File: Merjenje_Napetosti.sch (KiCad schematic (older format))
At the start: 6 parts

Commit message: Dodano vezje za OC_trip pri merjenju toka
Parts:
- removed U?: MCP6001R, Package_TO_SOT_SMD:SOT-23-5, symbol Amplifier_Operational:MCP6001R
- added U?: MCP601R, Package_TO_SOT_SMD:SOT-23-5, symbol Amplifier_Operational:MCP601R
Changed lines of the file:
@@
 $Descr A4 11693 8268
 encoding utf-8
-Sheet 4 4
+Sheet 4 5
 Title ""
 Date ""
@@
 	3500 2800 4250 2800
 $Comp
-L Amplifier_Operational:MCP6001R U?
-U 1 1 5BCCC475
-P 5050 2450
-F 0 "U?" H 5391 2496 50  0000 L CNN
-F 1 "MCP6001R" H 5391 2405 50  0000 L CNN
-F 2 "Package_TO_SOT_SMD:SOT-23-5" H 5050 2450 50  0001 C CNN
-F 3 "http://ww1.microchip.com/downloads/en/DeviceDoc/21733j.pdf" H 5050 2650 50  0001 C CNN
-	1    5050 2450
-	1    0    0    -1
-$EndComp
-$Comp
 L Passives:GND #PWR?
 U 1 1 5BCCC5E3
@@
 Wire Wire Line
 	5450 2450 5800 2450
+$Comp
+L Amplifier_Operational:MCP601R U?
+U 1 1 5BCDCCEB
+P 5050 2450
+F 0 "U?" H 5391 2496 50  0000 L CNN
+F 1 "MCP601R" H 5391 2405 50  0000 L CNN
+F 2 "Package_TO_SOT_SMD:SOT-23-5" H 5050 2450 50  0001 C CNN
+F 3 "http://ww1.microchip.com/downloads/en/DeviceDoc/21314g.pdf" H 5050 2650 50  0001 C CNN
+	1    5050 2450
+	1    0    0    -1
+$EndComp
 $EndSCHEMATC

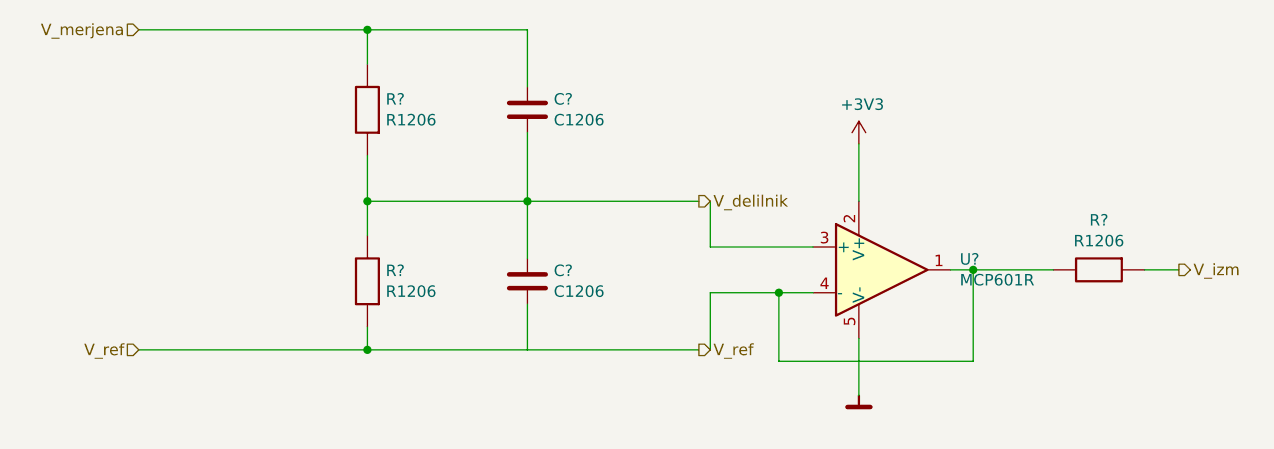
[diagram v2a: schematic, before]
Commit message: Naredil še sheet napajanje in popravil merilnik napetosti pri merjenju fazne napetosti
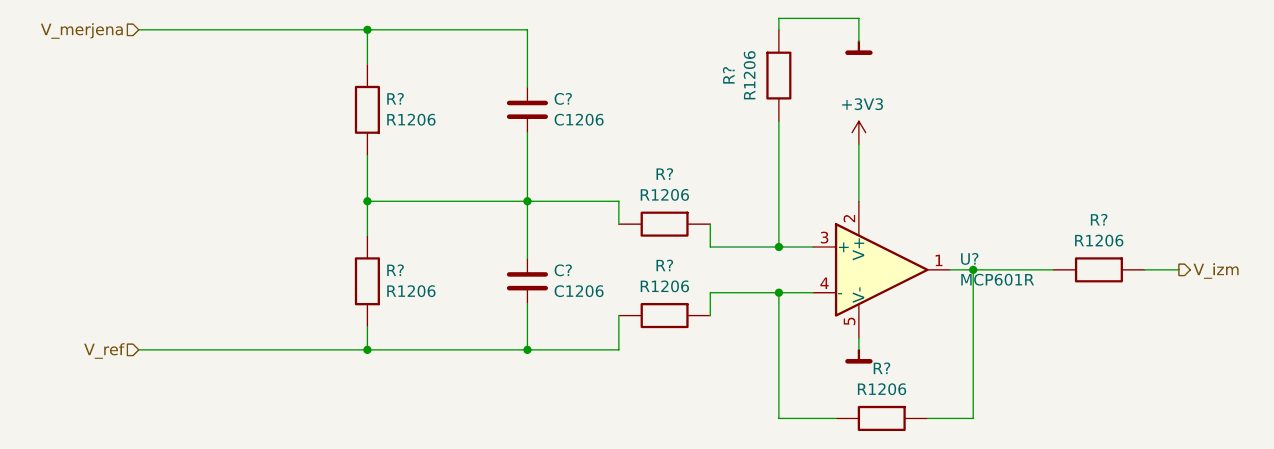
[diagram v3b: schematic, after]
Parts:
- removed U?: MCP601R, Package_TO_SOT_SMD:SOT-23-5, symbol Amplifier_Operational:MCP601R
- added R? (x4): R1206, Passives:R1206M, symbol Passives:R1206
- added U?: MCP601R, Package_TO_SOT_SMD:SOT-23-5, symbol Amplifier_Operational:MCP601R
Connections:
- net labels removed: V_delilnik
- wire segments 28 -> 36
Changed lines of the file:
@@
 $Descr A4 11693 8268
 encoding utf-8
-Sheet 4 7
+Sheet 4 9
 Title ""
 Date ""
@@
 U 1 1 5BCCBE50
 P 2800 1750
+AR Path="/5BC702AD/5BCCBCD0/5BCCBE50" Ref="R?"  Part="1"
+AR Path="/5BD3A78C/5BCCBE50" Ref="R?"  Part="1"
 F 0 "R?" V 2754 1830 50  0000 L CNN
 F 1 "R1206" V 2845 1830 50  0000 L CNN
@@
 U 1 1 5BCCBFA4
 P 2800 2500
+AR Path="/5BC702AD/5BCCBCD0/5BCCBFA4" Ref="R?"  Part="1"
+AR Path="/5BD3A78C/5BCCBFA4" Ref="R?"  Part="1"
 F 0 "R?" V 2754 2580 50  0000 L CNN
 F 1 "R1206" V 2845 2580 50  0000 L CNN
@@
 U 1 1 5BCCBFDD
 P 3500 1750
+AR Path="/5BC702AD/5BCCBCD0/5BCCBFDD" Ref="C?"  Part="1"
+AR Path="/5BD3A78C/5BCCBFDD" Ref="C?"  Part="1"
 F 0 "C?" H 3615 1796 50  0000 L CNN
 F 1 "C1206" H 3615 1705 50  0000 L CNN
@@
 U 1 1 5BCCC057
 P 3500 2500
+AR Path="/5BC702AD/5BCCBCD0/5BCCC057" Ref="C?"  Part="1"
+AR Path="/5BD3A78C/5BCCC057" Ref="C?"  Part="1"
 F 0 "C?" H 3615 2546 50  0000 L CNN
 F 1 "C1206" H 3615 2455 50  0000 L CNN
@@
 Wire Wire Line
 	3500 2800 3500 2600
-Text HLabel 1800 1400 0    50   Input ~ 0
-V_merjena
 Wire Wire Line
 	1800 1400 2800 1400
 Connection ~ 2800 1400
-Text HLabel 1800 2800 0    50   Input ~ 0
-V_ref
 Wire Wire Line
 	2800 2800 1800 2800
@@
 Wire Wire Line
 	3500 2150 3500 2400
-Text HLabel 4250 2150 2    50   Output ~ 0
-V_delilnik
-Wire Wire Line
-	3500 2150 4250 2150
-Text HLabel 4250 2800 2    50   Output ~ 0
-V_ref
-Wire Wire Line
-	3500 2800 4250 2800
-$Comp
-L Passives:GND #PWR?
-U 1 1 5BCCC5E3
-P 4950 3000
-F 0 "#PWR?" H 4950 2850 50  0001 C CNN
-F 1 "GND" H 5100 2950 50  0001 C CNN
-F 2 "" H 4950 3000 50  0001 C CNN
-F 3 "" H 4950 3000 50  0001 C CNN
-	1    4950 3000
-	1    0    0    -1
-$EndComp
-Wire Wire Line
-	4950 2750 4950 3000
-Wire Wire Line
-	4300 2800 4300 2550
-Wire Wire Line
-	4300 2550 4600 2550
-Wire Wire Line
-	4300 2150 4300 2350
-Wire Wire Line
-	4300 2350 4750 2350
 $Comp
 L Passives:R1206 R?
 U 1 1 5BCCC942
 P 6000 2450
+AR Path="/5BC702AD/5BCCBCD0/5BCCC942" Ref="R?"  Part="1"
+AR Path="/5BD3A78C/5BCCC942" Ref="R?"  Part="1"
 F 0 "R?" H 6000 2667 50  0000 C CNN
 F 1 "R1206" H 6000 2576 50  0000 C CNN
@@
 	1    0    0    -1
 $EndComp
-Wire Wire Line
-	5350 2450 5450 2450
 Text HLabel 6350 2450 2    50   Output ~ 0
 V_izm
 Wire Wire Line
 	6200 2450 6350 2450
+Text HLabel 1800 2800 0    50   Input ~ 0
+V_ref
+Text HLabel 1800 1400 0    50   Input ~ 0
+V_merjena
+$Comp
+L Passives:GND #PWR?
+U 1 1 5BD45445
+P 4950 2800
+AR Path="/5BC702AD/5BCCBCD0/5BD45445" Ref="#PWR?"  Part="1"
+AR Path="/5BD3A78C/5BD45445" Ref="#PWR?"  Part="1"
+F 0 "#PWR?" H 4950 2650 50  0001 C CNN
+F 1 "GND" H 5100 2750 50  0001 C CNN
+F 2 "" H 4950 2800 50  0001 C CNN
+F 3 "" H 4950 2800 50  0001 C CNN
+	1    4950 2800
+	1    0    0    -1
+$EndComp
+Wire Wire Line
+	4300 2550 4600 2550
+Wire Wire Line
+	4300 2350 4600 2350
+Wire Wire Line
+	5350 2450 5450 2450
 $Comp
 L power:+3V3 #PWR?
-U 1 1 5BCCD420
+U 1 1 5BD4544E
 P 4950 1900
+AR Path="/5BC702AD/5BCCBCD0/5BD4544E" Ref="#PWR?"  Part="1"
+AR Path="/5BD3A78C/5BD4544E" Ref="#PWR?"  Part="1"
 F 0 "#PWR?" H 4950 1750 50  0001 C CNN
 F 1 "+3V3" H 4965 2073 50  0000 C CNN
@@
 Wire Wire Line
 	4950 1900 4950 2150
-Wire Wire Line
-	4600 2550 4600 2850
-Wire Wire Line
-	4600 2850 5450 2850
-Wire Wire Line
-	5450 2850 5450 2450
 Connection ~ 4600 2550
 Wire Wire Line
@@
 $Comp
 L Amplifier_Operational:MCP601R U?
-U 1 1 5BCDCCEB
+U 1 1 5BD45459
 P 5050 2450
+AR Path="/5BC702AD/5BCCBCD0/5BD45459" Ref="U?"  Part="1"
+AR Path="/5BD3A78C/5BD45459" Ref="U?"  Part="1"
 F 0 "U?" H 5391 2496 50  0000 L CNN
 F 1 "MCP601R" H 5391 2405 50  0000 L CNN
@@
 	1    0    0    -1
 $EndComp
+$Comp
+L Passives:R1206 R?
+U 1 1 5BD45460
+P 4100 2250
+AR Path="/5BC702AD/5BCCBCD0/5BD45460" Ref="R?"  Part="1"
+AR Path="/5BD3A78C/5BD45460" Ref="R?"  Part="1"
+F 0 "R?" H 4100 2467 50  0000 C CNN
+F 1 "R1206" H 4100 2376 50  0000 C CNN
+F 2 "Passives:R1206M" H 4000 2150 50  0001 L CNN
+F 3 "" H 4100 2250 50  0001 C CNN
+	1    4100 2250
+	1    0    0    -1
+$EndComp
+$Comp
+L Passives:R1206 R?
+U 1 1 5BD45468
+P 4600 1600
+AR Path="/5BC702AD/5BCCBCD0/5BD45468" Ref="R?"  Part="1"
+AR Path="/5BD3A78C/5BD45468" Ref="R?"  Part="1"
+F 0 "R?" H 4600 1817 50  0000 C CNN
+F 1 "R1206" H 4600 1726 50  0000 C CNN
+F 2 "Passives:R1206M" H 4500 1500 50  0001 L CNN
+F 3 "" H 4600 1600 50  0001 C CNN
+	1    4600 1600
+	0    -1   -1   0
+$EndComp
+Wire Wire Line
+	4600 2350 4600 1800
+Connection ~ 4600 2350
+Wire Wire Line
+	4600 2350 4750 2350
+$Comp
+L Passives:GND #PWR?
+U 1 1 5BD45472
+P 4950 1450
+F 0 "#PWR?" H 4950 1300 50  0001 C CNN
+F 1 "GND" H 5100 1400 50  0001 C CNN
+F 2 "" H 4950 1450 50  0001 C CNN
+F 3 "" H 4950 1450 50  0001 C CNN
+	1    4950 1450
+	1    0    0    -1
+$EndComp
+Wire Wire Line
+	4950 1450 4950 1350
+Wire Wire Line
+	4950 1350 4600 1350
+Wire Wire Line
+	4600 1350 4600 1400
+$Comp
+L Passives:R1206 R?
+U 1 1 5BD4547B
+P 5050 3100
+AR Path="/5BC702AD/5BCCBCD0/5BD4547B" Ref="R?"  Part="1"
+AR Path="/5BD3A78C/5BD4547B" Ref="R?"  Part="1"
+F 0 "R?" H 5050 3317 50  0000 C CNN
+F 1 "R1206" H 5050 3226 50  0000 C CNN
+F 2 "Passives:R1206M" H 4950 3000 50  0001 L CNN
+F 3 "" H 5050 3100 50  0001 C CNN
+	1    5050 3100
+	1    0    0    -1
+$EndComp
+Wire Wire Line
+	4850 3100 4600 3100
+Wire Wire Line
+	5450 3100 5250 3100
+Wire Wire Line
+	4950 2800 4950 2750
+Wire Wire Line
+	4600 2550 4600 3100
+Wire Wire Line
+	5450 2450 5450 3100
+$Comp
+L Passives:R1206 R?
+U 1 1 5BD45487
+P 4100 2650
+AR Path="/5BC702AD/5BCCBCD0/5BD45487" Ref="R?"  Part="1"
+AR Path="/5BD3A78C/5BD45487" Ref="R?"  Part="1"
+F 0 "R?" H 4100 2867 50  0000 C CNN
+F 1 "R1206" H 4100 2776 50  0000 C CNN
+F 2 "Passives:R1206M" H 4000 2550 50  0001 L CNN
+F 3 "" H 4100 2650 50  0001 C CNN
+	1    4100 2650
+	1    0    0    -1
+$EndComp
+Wire Wire Line
+	4300 2350 4300 2250
+Wire Wire Line
+	4300 2650 4300 2550
+Wire Wire Line
+	3500 2150 3900 2150
+Wire Wire Line
+	3900 2150 3900 2250
+Wire Wire Line
+	3500 2800 3900 2800
+Wire Wire Line
+	3900 2800 3900 2650
+Connection ~ 3500 2800
 $EndSCHEMATC

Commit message: Dodal nekaj blikornih kondenzatorjev
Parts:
- removed R? (x4): R1206, Passives:R1206M, symbol Passives:R1206
- added C?: C1206, Passives:C1206M, symbol Passives:C1206
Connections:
- net V_ref is gone; now on net GND: C?.2, R?.2
- net +3V3: now also C?.1
- net GND: now also C?.2
- net at C?.1, C?.2, R?.1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: now also U?.3 (+)
- net at R?.1, U?.1: now also U?.4 (-)
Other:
- moved on the sheet: R?, U?
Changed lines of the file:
@@
 L Passives:R1206 R?
 U 1 1 5BCCC942
-P 6000 2450
+P 6000 2250
 AR Path="/5BC702AD/5BCCBCD0/5BCCC942" Ref="R?"  Part="1"
 AR Path="/5BD3A78C/5BCCC942" Ref="R?"  Part="1"
-F 0 "R?" H 6000 2667 50  0000 C CNN
-F 1 "R1206" H 6000 2576 50  0000 C CNN
-F 2 "Passives:R1206M" H 5900 2350 50  0001 L CNN
-F 3 "" H 6000 2450 50  0001 C CNN
-	1    6000 2450
+F 0 "R?" H 6000 2467 50  0000 C CNN
+F 1 "R1206" H 6000 2376 50  0000 C CNN
+F 2 "Passives:R1206M" H 5900 2150 50  0001 L CNN
+F 3 "" H 6000 2250 50  0001 C CNN
+	1    6000 2250
 	1    0    0    -1
 $EndComp
-Text HLabel 6350 2450 2    50   Output ~ 0
+Text HLabel 6350 2250 2    50   Output ~ 0
 V_izm
 Wire Wire Line
-	6200 2450 6350 2450
-Text HLabel 1800 2800 0    50   Input ~ 0
-V_ref
+	6200 2250 6350 2250
 Text HLabel 1800 1400 0    50   Input ~ 0
 V_merjena
@@
 $EndComp
 Wire Wire Line
-	4300 2550 4600 2550
-Wire Wire Line
-	4300 2350 4600 2350
-Wire Wire Line
-	5350 2450 5450 2450
+	5350 2250 5450 2250
 $Comp
 L power:+3V3 #PWR?
 U 1 1 5BD4544E
-P 4950 1900
+P 4950 1700
 AR Path="/5BC702AD/5BCCBCD0/5BD4544E" Ref="#PWR?"  Part="1"
 AR Path="/5BD3A78C/5BD4544E" Ref="#PWR?"  Part="1"
-F 0 "#PWR?" H 4950 1750 50  0001 C CNN
-F 1 "+3V3" H 4965 2073 50  0000 C CNN
-F 2 "" H 4950 1900 50  0001 C CNN
-F 3 "" H 4950 1900 50  0001 C CNN
-	1    4950 1900
+F 0 "#PWR?" H 4950 1550 50  0001 C CNN
+F 1 "+3V3" H 4965 1873 50  0000 C CNN
+F 2 "" H 4950 1700 50  0001 C CNN
+F 3 "" H 4950 1700 50  0001 C CNN
+	1    4950 1700
 	1    0    0    -1
 $EndComp
 Wire Wire Line
-	4950 1900 4950 2150
-Connection ~ 4600 2550
+	4950 1700 4950 1850
 Wire Wire Line
-	4600 2550 4750 2550
-Connection ~ 5450 2450
+	4600 2350 4750 2350
+Connection ~ 5450 2250
 Wire Wire Line
-	5450 2450 5800 2450
+	5450 2250 5800 2250
 $Comp
 L Amplifier_Operational:MCP601R U?
 U 1 1 5BD45459
-P 5050 2450
+P 5050 2250
 AR Path="/5BC702AD/5BCCBCD0/5BD45459" Ref="U?"  Part="1"
 AR Path="/5BD3A78C/5BD45459" Ref="U?"  Part="1"
-F 0 "U?" H 5391 2496 50  0000 L CNN
-F 1 "MCP601R" H 5391 2405 50  0000 L CNN
-F 2 "Package_TO_SOT_SMD:SOT-23-5" H 5050 2450 50  0001 C CNN
-F 3 "http://ww1.microchip.com/downloads/en/DeviceDoc/21314g.pdf" H 5050 2650 50  0001 C CNN
-	1    5050 2450
-	1    0    0    -1
-$EndComp
-$Comp
-L Passives:R1206 R?
-U 1 1 5BD45460
-P 4100 2250
-AR Path="/5BC702AD/5BCCBCD0/5BD45460" Ref="R?"  Part="1"
-AR Path="/5BD3A78C/5BD45460" Ref="R?"  Part="1"
-F 0 "R?" H 4100 2467 50  0000 C CNN
-F 1 "R1206" H 4100 2376 50  0000 C CNN
-F 2 "Passives:R1206M" H 4000 2150 50  0001 L CNN
-F 3 "" H 4100 2250 50  0001 C CNN
-	1    4100 2250
-	1    0    0    -1
-$EndComp
-$Comp
-L Passives:R1206 R?
-U 1 1 5BD45468
-P 4600 1600
-AR Path="/5BC702AD/5BCCBCD0/5BD45468" Ref="R?"  Part="1"
-AR Path="/5BD3A78C/5BD45468" Ref="R?"  Part="1"
-F 0 "R?" H 4600 1817 50  0000 C CNN
-F 1 "R1206" H 4600 1726 50  0000 C CNN
-F 2 "Passives:R1206M" H 4500 1500 50  0001 L CNN
-F 3 "" H 4600 1600 50  0001 C CNN
-	1    4600 1600
-	0    -1   -1   0
-$EndComp
-Wire Wire Line
-	4600 2350 4600 1800
-Connection ~ 4600 2350
-Wire Wire Line
-	4600 2350 4750 2350
-$Comp
-L Passives:GND #PWR?
-U 1 1 5BD45472
-P 4950 1450
-F 0 "#PWR?" H 4950 1300 50  0001 C CNN
-F 1 "GND" H 5100 1400 50  0001 C CNN
-F 2 "" H 4950 1450 50  0001 C CNN
-F 3 "" H 4950 1450 50  0001 C CNN
-	1    4950 1450
+F 0 "U?" H 5391 2296 50  0000 L CNN
+F 1 "MCP601R" H 5391 2205 50  0000 L CNN
+F 2 "Package_TO_SOT_SMD:SOT-23-5" H 5050 2250 50  0001 C CNN
+F 3 "http://ww1.microchip.com/downloads/en/DeviceDoc/21314g.pdf" H 5050 2450 50  0001 C CNN
+	1    5050 2250
 	1    0    0    -1
 $EndComp
 Wire Wire Line
-	4950 1450 4950 1350
+	4600 3100 5450 3100
 Wire Wire Line
-	4950 1350 4600 1350
-Wire Wire Line
-	4600 1350 4600 1400
+	3500 2150 4750 2150
 $Comp
-L Passives:R1206 R?
-U 1 1 5BD4547B
-P 5050 3100
-AR Path="/5BC702AD/5BCCBCD0/5BD4547B" Ref="R?"  Part="1"
-AR Path="/5BD3A78C/5BD4547B" Ref="R?"  Part="1"
-F 0 "R?" H 5050 3317 50  0000 C CNN
-F 1 "R1206" H 5050 3226 50  0000 C CNN
-F 2 "Passives:R1206M" H 4950 3000 50  0001 L CNN
-F 3 "" H 5050 3100 50  0001 C CNN
-	1    5050 3100
+L Passives:GND #PWR?
+U 1 1 5BDBD8E9
+P 1800 2950
+F 0 "#PWR?" H 1800 2800 50  0001 C CNN
+F 1 "GND" H 1950 2900 50  0001 C CNN
+F 2 "" H 1800 2950 50  0001 C CNN
+F 3 "" H 1800 2950 50  0001 C CNN
+	1    1800 2950
 	1    0    0    -1
 $EndComp
 Wire Wire Line
-	4850 3100 4600 3100
+	1800 2950 1800 2800
 Wire Wire Line
-	5450 3100 5250 3100
+	5450 2250 5450 3100
 Wire Wire Line
-	4950 2800 4950 2750
-Wire Wire Line
-	4600 2550 4600 3100
-Wire Wire Line
-	5450 2450 5450 3100
+	4600 2350 4600 3100
 $Comp
-L Passives:R1206 R?
-U 1 1 5BD45487
-P 4100 2650
-AR Path="/5BC702AD/5BCCBCD0/5BD45487" Ref="R?"  Part="1"
-AR Path="/5BD3A78C/5BD45487" Ref="R?"  Part="1"
-F 0 "R?" H 4100 2867 50  0000 C CNN
-F 1 "R1206" H 4100 2776 50  0000 C CNN
-F 2 "Passives:R1206M" H 4000 2550 50  0001 L CNN
-F 3 "" H 4100 2650 50  0001 C CNN
-	1    4100 2650
+L Passives:C1206 C?
+U 1 1 5BE2B7C3
+P 5300 2600
+F 0 "C?" H 5415 2646 50  0000 L CNN
+F 1 "C1206" H 5415 2555 50  0000 L CNN
+F 2 "Passives:C1206M" H 5350 2500 50  0001 L CNN
+F 3 "" H 5300 2600 50  0001 C CNN
+	1    5300 2600
 	1    0    0    -1
 $EndComp
 Wire Wire Line
-	4300 2350 4300 2250
+	4950 2550 4950 2750
 Wire Wire Line
-	4300 2650 4300 2550
+	4950 2750 5300 2750
 Wire Wire Line
-	3500 2150 3900 2150
+	5300 2750 5300 2700
+Connection ~ 4950 2750
 Wire Wire Line
-	3900 2150 3900 2250
+	4950 2750 4950 2800
 Wire Wire Line
-	3500 2800 3900 2800
+	5300 1850 4950 1850
 Wire Wire Line
-	3900 2800 3900 2650
-Connection ~ 3500 2800
+	5300 1850 5300 2500
+Connection ~ 4950 1850
+Wire Wire Line
+	4950 1850 4950 1950
 $EndSCHEMATC
